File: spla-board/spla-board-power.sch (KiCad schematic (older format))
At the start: 17 parts, among them J10 J_3V3_EN, J11 J_5V_SWITCH, J12 J_POWER, J7 Barrel_Jack, J8 J_3V3_EN, J9 J_2V5_EN, U14 TLV73311PDBV, U7 MIC2025-1YM, U8 TLV73333PDBV, U9 TLV73325PDBV

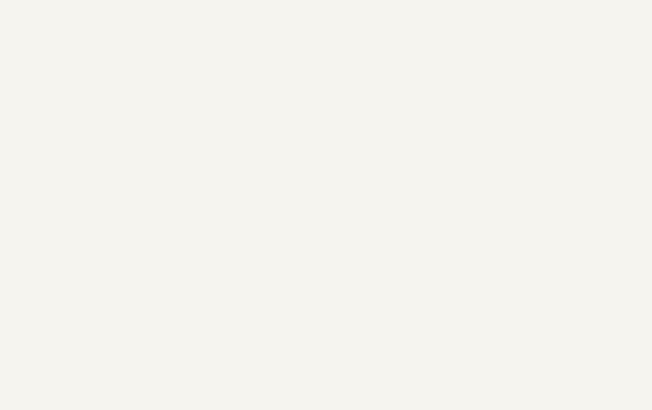
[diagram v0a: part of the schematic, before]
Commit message: pcb/schematic: Add plated mounting holes.
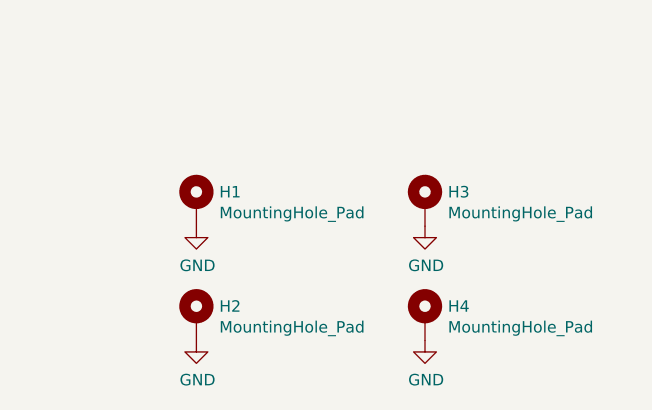
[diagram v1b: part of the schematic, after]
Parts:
- added H1, H2, H3, H4: MountingHole_Pad, MountingHole:MountingHole_3.2mm_M3_Pad, symbol Mechanical:MountingHole_Pad
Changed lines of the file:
@@
 Text Notes 3900 5600 0    50   ~ 0
 TODO: Swap these 300mA LDOs for AMS1117 parts.
+$Comp
+L Mechanical:MountingHole_Pad H?
+U 1 1 5E9F55D4
+P 13400 8150
+AR Path="/5E9F55D4" Ref="H?"  Part="1"
+AR Path="/5E50D39B/5E9F55D4" Ref="H1"  Part="1"
+F 0 "H1" H 13500 8199 50  0000 L CNN
+F 1 "MountingHole_Pad" H 13500 8108 50  0000 L CNN
+F 2 "MountingHole:MountingHole_3.2mm_M3_Pad" H 13400 8150 50  0001 C CNN
+F 3 "~" H 13400 8150 50  0001 C CNN
+	1    13400 8150
+	1    0    0    -1
+$EndComp
+$Comp
+L Mechanical:MountingHole_Pad H?
+U 1 1 5E9F55DA
+P 14400 8150
+AR Path="/5E9F55DA" Ref="H?"  Part="1"
+AR Path="/5E50D39B/5E9F55DA" Ref="H3"  Part="1"
+F 0 "H3" H 14500 8199 50  0000 L CNN
+F 1 "MountingHole_Pad" H 14500 8108 50  0000 L CNN
+F 2 "MountingHole:MountingHole_3.2mm_M3_Pad" H 14400 8150 50  0001 C CNN
+F 3 "~" H 14400 8150 50  0001 C CNN
+	1    14400 8150
+	1    0    0    -1
+$EndComp
+$Comp
+L Mechanical:MountingHole_Pad H?
+U 1 1 5E9F55E0
+P 13400 8650
+AR Path="/5E9F55E0" Ref="H?"  Part="1"
+AR Path="/5E50D39B/5E9F55E0" Ref="H2"  Part="1"
+F 0 "H2" H 13500 8699 50  0000 L CNN
+F 1 "MountingHole_Pad" H 13500 8608 50  0000 L CNN
+F 2 "MountingHole:MountingHole_3.2mm_M3_Pad" H 13400 8650 50  0001 C CNN
+F 3 "~" H 13400 8650 50  0001 C CNN
+	1    13400 8650
+	1    0    0    -1
+$EndComp
+$Comp
+L Mechanical:MountingHole_Pad H?
+U 1 1 5E9F55E6
+P 14400 8650
+AR Path="/5E9F55E6" Ref="H?"  Part="1"
+AR Path="/5E50D39B/5E9F55E6" Ref="H4"  Part="1"
+F 0 "H4" H 14500 8699 50  0000 L CNN
+F 1 "MountingHole_Pad" H 14500 8608 50  0000 L CNN
+F 2 "MountingHole:MountingHole_3.2mm_M3_Pad" H 14400 8650 50  0001 C CNN
+F 3 "~" H 14400 8650 50  0001 C CNN
+	1    14400 8650
+	1    0    0    -1
+$EndComp
+$Comp
+L power:GND #PWR?
+U 1 1 5E9F55EC
+P 13400 8250
+AR Path="/5E9F55EC" Ref="#PWR?"  Part="1"
+AR Path="/5E50D39B/5E9F55EC" Ref="#PWR0176"  Part="1"
+F 0 "#PWR0176" H 13400 8000 50  0001 C CNN
+F 1 "GND" H 13405 8077 50  0000 C CNN
+F 2 "" H 13400 8250 50  0001 C CNN
+F 3 "" H 13400 8250 50  0001 C CNN
+	1    13400 8250
+	1    0    0    -1
+$EndComp
+$Comp
+L power:GND #PWR?
+U 1 1 5E9F55F2
+P 14400 8250
+AR Path="/5E9F55F2" Ref="#PWR?"  Part="1"
+AR Path="/5E50D39B/5E9F55F2" Ref="#PWR0180"  Part="1"
+F 0 "#PWR0180" H 14400 8000 50  0001 C CNN
+F 1 "GND" H 14405 8077 50  0000 C CNN
+F 2 "" H 14400 8250 50  0001 C CNN
+F 3 "" H 14400 8250 50  0001 C CNN
+	1    14400 8250
+	1    0    0    -1
+$EndComp
+$Comp
+L power:GND #PWR?
+U 1 1 5E9F55F8
+P 13400 8750
+AR Path="/5E9F55F8" Ref="#PWR?"  Part="1"
+AR Path="/5E50D39B/5E9F55F8" Ref="#PWR0181"  Part="1"
+F 0 "#PWR0181" H 13400 8500 50  0001 C CNN
+F 1 "GND" H 13405 8577 50  0000 C CNN
+F 2 "" H 13400 8750 50  0001 C CNN
+F 3 "" H 13400 8750 50  0001 C CNN
+	1    13400 8750
+	1    0    0    -1
+$EndComp
+$Comp
+L power:GND #PWR?
+U 1 1 5E9F55FE
+P 14400 8750
+AR Path="/5E9F55FE" Ref="#PWR?"  Part="1"
+AR Path="/5E50D39B/5E9F55FE" Ref="#PWR0184"  Part="1"
+F 0 "#PWR0184" H 14400 8500 50  0001 C CNN
+F 1 "GND" H 14405 8577 50  0000 C CNN
+F 2 "" H 14400 8750 50  0001 C CNN
+F 3 "" H 14400 8750 50  0001 C CNN
+	1    14400 8750
+	1    0    0    -1
+$EndComp
 $EndSCHEMATC

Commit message: symbol/footprint/schematic: Redo power entirely to use ST1S10 and TLV733 parts.
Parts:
- removed J10, J8: J_3V3_EN, Connector_PinHeader_2.54mm:PinHeader_2x03_P2.54mm_Vertical, symbol Connector_Generic:Conn_02x03_Odd_Even
- removed J11: J_5V_SWITCH, Connector_PinHeader_2.54mm:PinHeader_2x03_P2.54mm_Vertical, symbol Connector_Generic:Conn_02x03_Odd_Even
- removed J9: J_2V5_EN, Connector_PinHeader_2.54mm:PinHeader_2x03_P2.54mm_Vertical, symbol Connector_Generic:Conn_02x03_Odd_Even
- removed TP6: TP_5V, TestPoint:TestPoint_Pad_D1.0mm, symbol Connector:TestPoint
- removed TP7: TP_3V3, TestPoint:TestPoint_Pad_D1.0mm, symbol Connector:TestPoint
- removed TP8: TP_2V5, TestPoint:TestPoint_Pad_D1.0mm, symbol Connector:TestPoint
- removed TP9: TP_1V1, TestPoint:TestPoint_Pad_D1.0mm, symbol Connector:TestPoint
- removed U7: MIC2025-1YM, Package_SO:SOIC-8_3.9x4.9mm_P1.27mm, symbol Power_Management:MIC2025-1YM
- removed U8: TLV73333PDBV, Package_TO_SOT_SMD:SOT-23-5, symbol Regulator_Linear:TLV73333PDBV
- added C28: 10uF, Capacitor_SMD:C_0805_2012Metric, symbol Device:C_Small
- added C29, C30, C31, C32, C35, C36, C41, C42: 0.1uF, Capacitor_SMD:C_0603_1608Metric, symbol Device:C_Small
- added C33, C34: 4.7uF, Capacitor_SMD:C_0603_1608Metric, symbol Device:C_Small
- added C37, C38, C39, C40: 22uF, Capacitor_SMD:C_0805_2012Metric, symbol Device:C_Small
- added L1, L2: 3.3uH, Inductor_SMD:L_Vishay_IHLP-2020, symbol Device:L
- added R26, R27, R28, R33, R34: 0, Resistor_SMD:R_0603_1608Metric, symbol Device:R_Small
- added R29: 5.23k, 1%, Resistor_SMD:R_0603_1608Metric, symbol Device:R_Small
- added R30, R32: 1k, 1%, Resistor_SMD:R_0603_1608Metric, symbol Device:R_Small
- added R31: 3.09k, 1%, Resistor_SMD:R_0603_1608Metric, symbol Device:R_Small
- added U7, U8: ST1S10PHR, SPLA:ST_PowerSO-8EP_4x5mm_P1.27mm_EP3.5x2.6mm, symbol SPLA:ST1S10PHR
- C13: value 0.1uF -> 10uF; footprint Capacitor_SMD:C_0603_1608Metric -> Capacitor_SMD:C_0805_2012Metric
- R12: value 10k -> 0
- TP5: value TP_5VD -> TP_12V
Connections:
- net labels added: +12V, PWR_12V, PWR_PRE_1V1, PWR_PRE_2V5, PWR_PRE_3V3, PWR_PRE_5V
- net labels removed: +5VD, PWR_5V_EN, PWR_OVERFLAG
- wire segments 99 -> 164
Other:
- note added: "SYNC = use internal 900kHz oscillator"
- note added: "V_OUT = ((0.8V / 1k) * 3.09k) + 0.8V = 3.272V"
- note added: "V_OUT = ((0.8V / 1k) * 5.23k) + 0.8V = 4.984V"
- note added: "~INH~ = Always On"
- note removed: "TODO: Swap these 300mA LDOs for AMS1117 parts."
- moved on the sheet: J12, J7, TP5

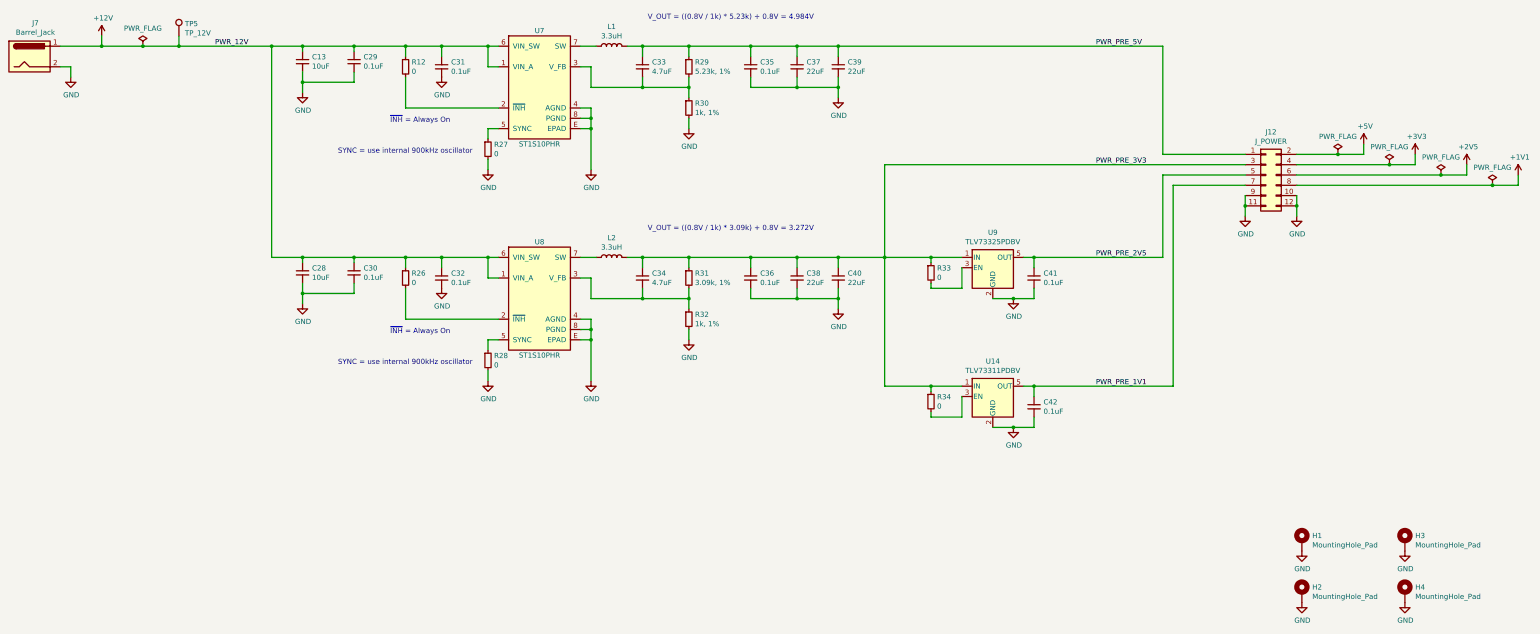
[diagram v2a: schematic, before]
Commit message: pcb/schematic: Partial work on power layout.
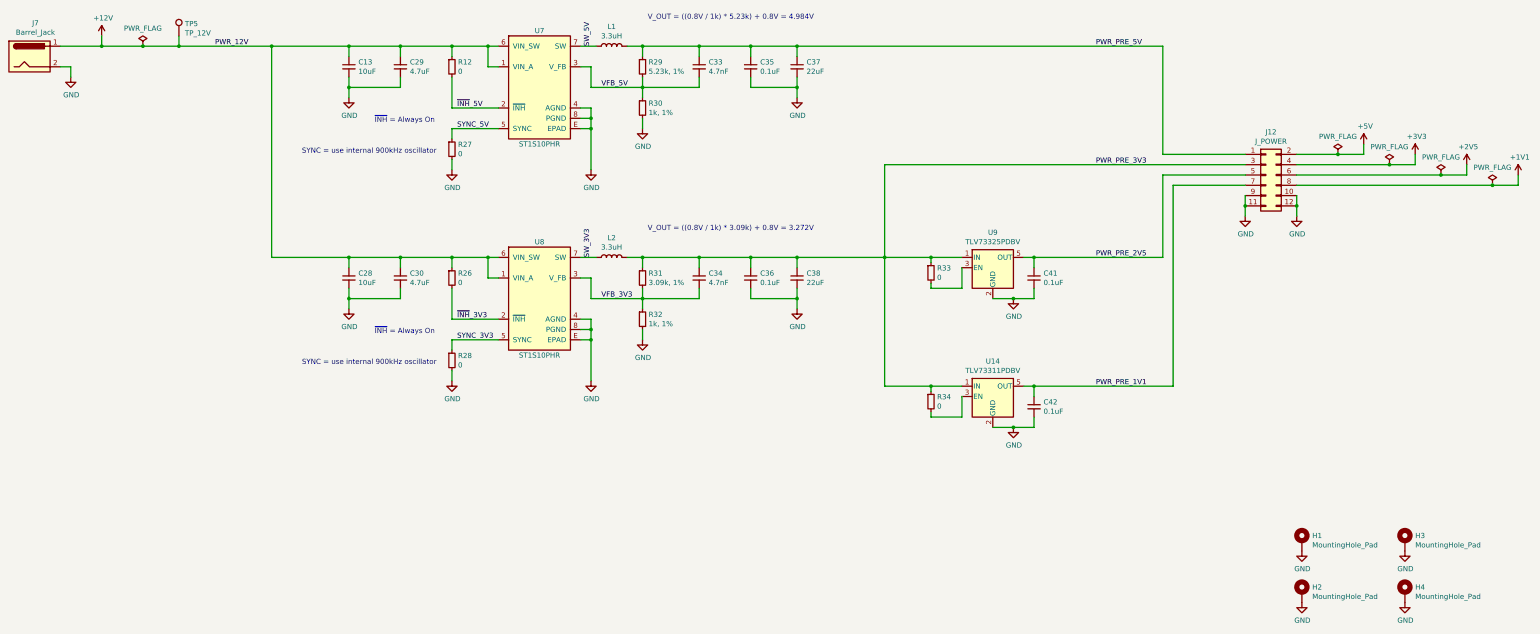
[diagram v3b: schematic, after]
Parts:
- removed C31, C32: 0.1uF, Capacitor_SMD:C_0603_1608Metric, symbol Device:C_Small
- removed C39, C40: 22uF, Capacitor_SMD:C_0805_2012Metric, symbol Device:C_Small
- C29, C30: value 0.1uF -> 4.7uF
- C33, C34: value 4.7uF -> 4.7nF
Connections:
- net ~INH~_5V: now reaches R12.2, U7.2 (~INH)
- net VFB_5V: now reaches C33.2, R29.2, R30.1, U7.3 (V_FB)
- net SYNC_5V: now reaches R27.1, U7.5 (SYNC)
- net SW_5V: now reaches L1.1, U7.7 (SW)
- net ~INH~_3V3: now reaches R26.2, U8.2 (~INH)
- net VFB_3V3: now reaches C34.2, R31.2, R32.1, U8.3 (V_FB)
- net SYNC_3V3: now reaches R28.1, U8.5 (SYNC)
- net SW_3V3: now reaches L2.1, U8.7 (SW)
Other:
- moved on the sheet: C13, C28, C29, C30, C33, C34, R12, R26, R27, R28, R29, R30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

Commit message: schematic/pcb: Rearrange 2.5V/1.1V jumpers; Move USB data liens to make space for power.
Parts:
- J12: footprint Connector_PinHeader_2.54mm:PinHeader_2x06_P2.54mm_Vertical -> Connector_PinHeader_2.54mm:PinHeader_2x07_P2.54mm_Vertical; symbol Connector_Generic:Conn_02x06_Odd_Even -> Connector_Generic:Conn_02x07_Odd_Even
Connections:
- net +1V1: now also C42.1, U14.5 (OUT); no longer J12.8 (Pin_8)
- net +2V5: now also C41.1, U9.5 (OUT); no longer J12.6 (Pin_6)
- net +3V3: now also J12.11 (Pin_11), J12.5 (Pin_5); no longer J12.4 (Pin_4)
- net +5V: now also J12.13 (Pin_13); no longer J12.2 (Pin_2)
- net GND: now also J12.1 (Pin_1), J12.2 (Pin_2), J12.3 (Pin_3), J12.4 (Pin_4); no longer J12.10 (Pin_10), J12.11 (Pin_11), J12.12 (Pin_12), J12.9 (Pin_9)
- net PWR_PRE_3V3: now also J12.10 (Pin_10), J12.12 (Pin_12), J12.6 (Pin_6), J12.8 (Pin_8); no longer J12.3 (Pin_3), R33.1, R34.1, U14.1 (IN), U9.1 (IN)
- net PWR_PRE_5V: now also J12.14 (Pin_14); no longer J12.1 (Pin_1)
- removed net PWR_PRE_1V1: C42.1, J12.7 (Pin_7), U14.5 (OUT)
- removed net PWR_PRE_2V5: C41.1, J12.5 (Pin_5), U9.5 (OUT)
- new net PWR_INTO_1V1: J12.7 (Pin_7), R34.1, U14.1 (IN)
- new net PWR_INTO_2V5: J12.9 (Pin_9), R33.1, U9.1 (IN)
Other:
- moved on the sheet: C41, C42, R33, R34, U14, U9

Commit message: pcb/schematic: Layout new power setup; tweak schematic to suit.
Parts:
- added TP6: TP_GND, TestPoint:TestPoint_Plated_Hole_D2.0mm, symbol Connector:TestPoint
- J12: footprint Connector_PinHeader_2.54mm:PinHeader_2x07_P2.54mm_Vertical -> Connector_PinHeader_2.54mm:PinHeader_2x08_P2.54mm_Vertical; symbol Connector_Generic:Conn_02x07_Odd_Even -> Connector_Generic:Conn_02x08_Odd_Even
- TP5: footprint TestPoint:TestPoint_Pad_D1.0mm -> TestPoint:TestPoint_Plated_Hole_D2.0mm
- renumbered C13 to C81, C37 to C82, C29 to C83, C33 to C84, C35 to C89, C28 to C91, C38 to C92, C30 to C93, C34 to C94, C36 to C99, R29 to R81, R30 to R82, R12 to R87, R27 to R88, R31 to R91, R32 to R92, R26 to R97, R28 to R98
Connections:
- net +3V3: now also J12.13 (Pin_13), J12.7 (Pin_7); no longer J12.11 (Pin_11), J12.5 (Pin_5)
- net +5V: now also J12.3 (Pin_3); no longer J12.13 (Pin_13)
- net GND: now also J12.15 (Pin_15), J12.16 (Pin_16), J12.5 (Pin_5), J12.6 (Pin_6), TP6.1; no longer J12.3 (Pin_3), J12.4 (Pin_4)
- net PWR_INTO_1V1: now also J12.11 (Pin_11); no longer J12.7 (Pin_7)
- net PWR_PRE_3V3: now also J12.14 (Pin_14); no longer J12.6 (Pin_6)
- net PWR_PRE_5V: now also J12.4 (Pin_4); no longer J12.14 (Pin_14)
- net PWR_EN_1V1: now reaches R34.2, U14.3 (EN)
- net PWR_EN_2V5: now reaches R33.2, U9.3 (EN)
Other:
- moved on the sheet: R33, R34

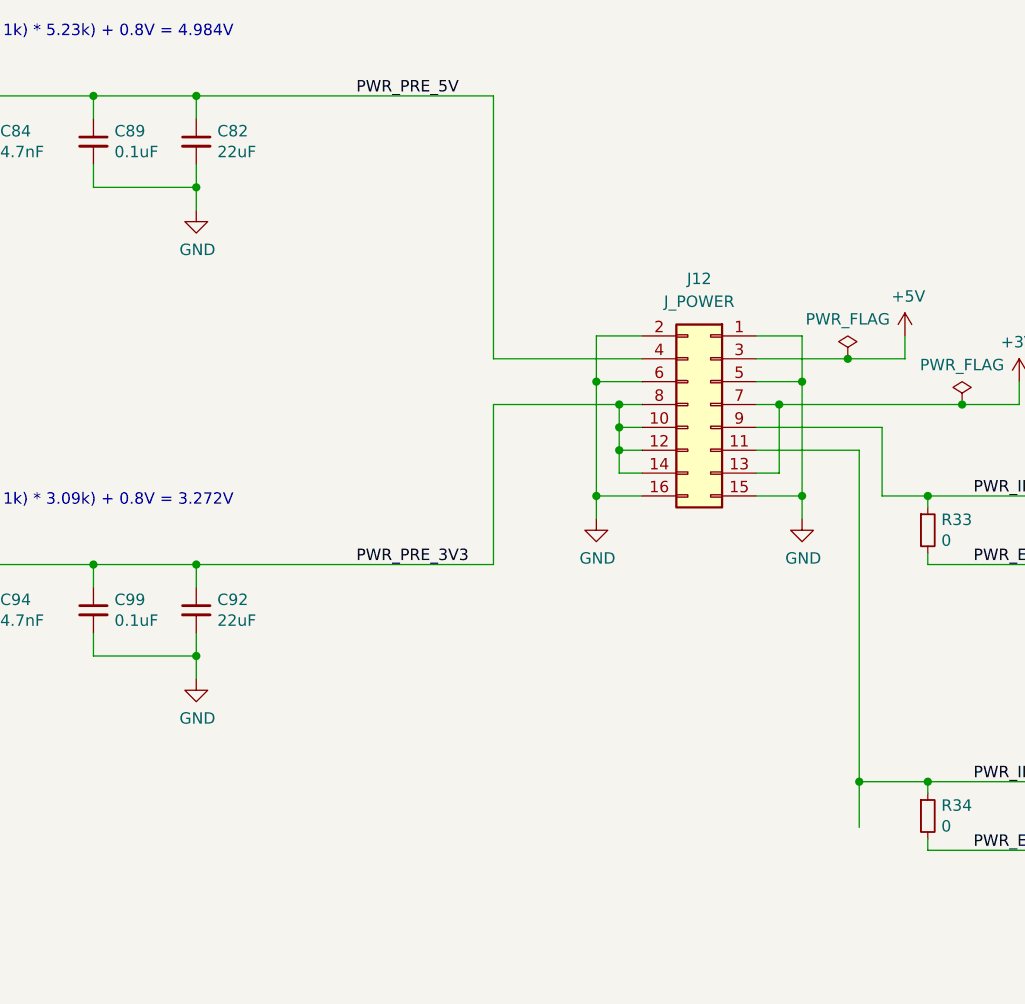
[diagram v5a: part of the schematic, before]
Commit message: schematic/pcb: Add LEDs to FTDI / FPGA / Power, for bringup and debugging.
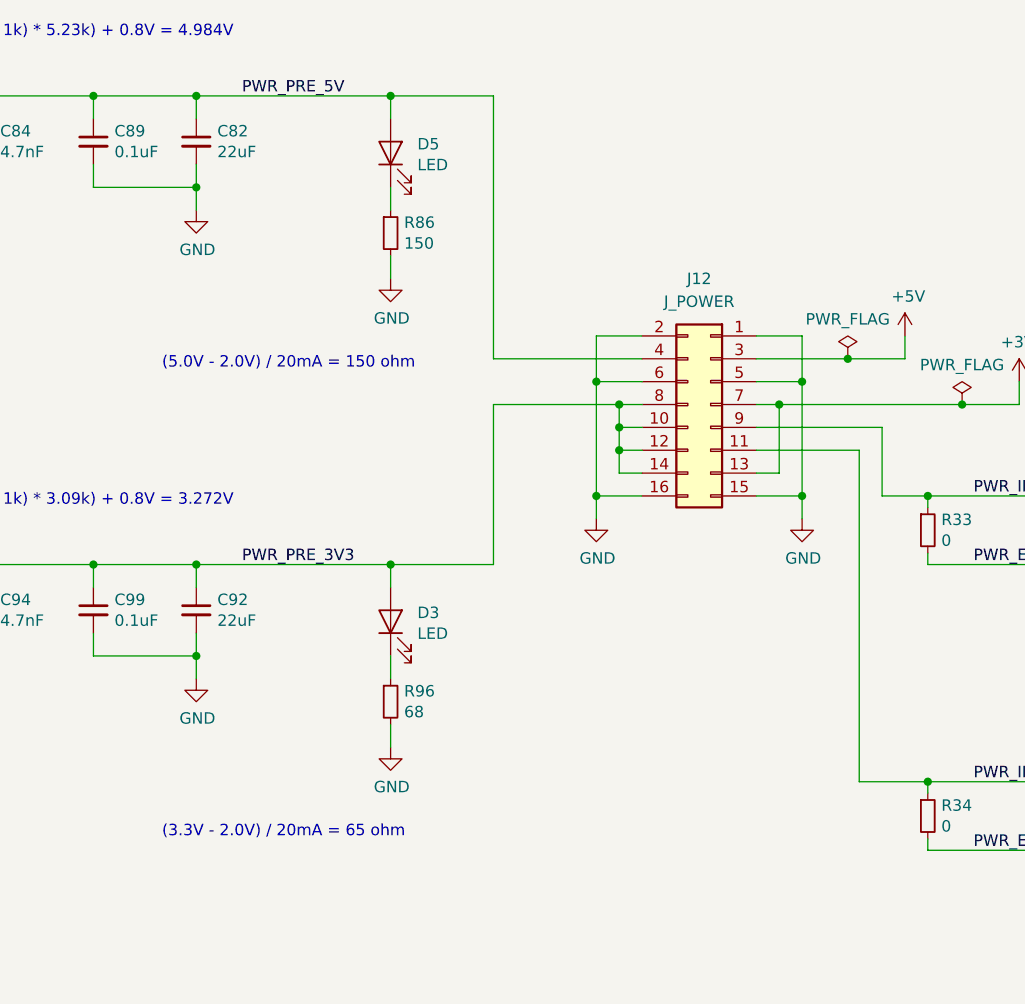
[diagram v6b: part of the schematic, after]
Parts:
- added D3, D5: LED, LED_SMD:LED_0805_2012Metric, symbol Device:LED
- added R86: 150, Resistor_SMD:R_0603_1608Metric, symbol Device:R_Small
- added R96: 68, Resistor_SMD:R_0603_1608Metric, symbol Device:R_Small
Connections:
- net GND: now also R86.2, R96.2
- net PWR_PRE_3V3: now also D3.2 (A)
- net PWR_PRE_5V: now also D5.2 (A)
- new net: D5.1 (K), R86.1
- new net: D3.1 (K), R96.1
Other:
- note added: "(3.3V - 2.0V) / 20mA = 65 ohm"
- note added: "(5.0V - 2.0V) / 20mA = 150 ohm"
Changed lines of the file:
@@
 Text Label 2850 3350 0    50   ~ 0
 PWR_12V
-Text Label 9200 3350 0    50   ~ 0
+Text Label 8700 3350 0    50   ~ 0
 PWR_PRE_5V
-Text Label 9200 5400 0    50   ~ 0
+Text Label 8700 5400 0    50   ~ 0
 PWR_PRE_3V3
 Wire Wire Line
@@
 	7000 3850 7000 3750
 Wire Wire Line
-	8500 3350 9800 3350
+	8500 3350 9350 3350
 Wire Wire Line
 	6500 5800 7000 5800
@@
 	8050 5800 8500 5800
 Wire Wire Line
-	8500 5400 9800 5400
+	8500 5400 9350 5400
 Wire Wire Line
 	10350 4900 10350 4800
@@
 Wire Wire Line
 	12100 4700 11850 4700
-Connection ~ 11400 6350
-Wire Wire Line
-	11400 6350 11400 6550
 Wire Wire Line
 	12100 4600 12100 4700
@@
 	2500 3650 1450 3650
 Connection ~ 2500 3650
+$Comp
+L Device:LED D?
+U 1 1 5EB36971
+P 9350 3600
+AR Path="/5E4F712F/5EB36971" Ref="D?"  Part="1"
+AR Path="/5E50D39B/5EB36971" Ref="D5"  Part="1"
+F 0 "D5" V 9389 3483 50  0000 R CNN
+F 1 "LED" V 9298 3483 50  0000 R CNN
+F 2 "LED_SMD:LED_0805_2012Metric" H 9350 3600 50  0001 C CNN
+F 3 "~" H 9350 3600 50  0001 C CNN
+	1    9350 3600
+	0    -1   -1   0
+$EndComp
+$Comp
+L Device:R_Small R?
+U 1 1 5EB36977
+P 9350 3950
+AR Path="/5E4F712F/5EB36977" Ref="R?"  Part="1"
+AR Path="/5E50D39B/5EB36977" Ref="R86"  Part="1"
+F 0 "R86" H 9409 3996 50  0000 L CNN
+F 1 "150" H 9409 3905 50  0000 L CNN
+F 2 "Resistor_SMD:R_0603_1608Metric" H 9350 3950 50  0001 C CNN
+F 3 "~" H 9350 3950 50  0001 C CNN
+	1    9350 3950
+	1    0    0    -1
+$EndComp
+Wire Wire Line
+	9350 3750 9350 3850
+Wire Wire Line
+	9350 4050 9350 4150
+$Comp
+L power:GND #PWR?
+U 1 1 5EB3697F
+P 9350 4150
+AR Path="/5E4F712F/5EB3697F" Ref="#PWR?"  Part="1"
+AR Path="/5E50D39B/5EB3697F" Ref="#PWR0190"  Part="1"
+F 0 "#PWR0190" H 9350 3900 50  0001 C CNN
+F 1 "GND" H 9355 3977 50  0000 C CNN
+F 2 "" H 9350 4150 50  0001 C CNN
+F 3 "" H 9350 4150 50  0001 C CNN
+	1    9350 4150
+	1    0    0    -1
+$EndComp
+Text Notes 8350 4550 0    50   ~ 0
+(5.0V - 2.0V) / 20mA = 150 ohm
+Wire Wire Line
+	9350 3350 9350 3450
+$Comp
+L Device:LED D?
+U 1 1 5EB3D482
+P 9350 5650
+AR Path="/5E4F712F/5EB3D482" Ref="D?"  Part="1"
+AR Path="/5E50D39B/5EB3D482" Ref="D3"  Part="1"
+F 0 "D3" V 9389 5533 50  0000 R CNN
+F 1 "LED" V 9298 5533 50  0000 R CNN
+F 2 "LED_SMD:LED_0805_2012Metric" H 9350 5650 50  0001 C CNN
+F 3 "~" H 9350 5650 50  0001 C CNN
+	1    9350 5650
+	0    -1   -1   0
+$EndComp
+$Comp
+L Device:R_Small R?
+U 1 1 5EB3D48C
+P 9350 6000
+AR Path="/5E4F712F/5EB3D48C" Ref="R?"  Part="1"
+AR Path="/5E50D39B/5EB3D48C" Ref="R96"  Part="1"
+F 0 "R96" H 9409 6046 50  0000 L CNN
+F 1 "68" H 9409 5955 50  0000 L CNN
+F 2 "Resistor_SMD:R_0603_1608Metric" H 9350 6000 50  0001 C CNN
+F 3 "~" H 9350 6000 50  0001 C CNN
+	1    9350 6000
+	1    0    0    -1
+$EndComp
+Wire Wire Line
+	9350 5800 9350 5900
+Wire Wire Line
+	9350 6100 9350 6200
+$Comp
+L power:GND #PWR?
+U 1 1 5EB3D498
+P 9350 6200
+AR Path="/5E4F712F/5EB3D498" Ref="#PWR?"  Part="1"
+AR Path="/5E50D39B/5EB3D498" Ref="#PWR0191"  Part="1"
+F 0 "#PWR0191" H 9350 5950 50  0001 C CNN
+F 1 "GND" H 9355 6027 50  0000 C CNN
+F 2 "" H 9350 6200 50  0001 C CNN
+F 3 "" H 9350 6200 50  0001 C CNN
+	1    9350 6200
+	1    0    0    -1
+$EndComp
+Text Notes 8350 6600 0    50   ~ 0
+(3.3V - 2.0V) / 20mA = 65 ohm
+Wire Wire Line
+	9350 5400 9350 5500
+Connection ~ 9350 5400
+Wire Wire Line
+	9350 5400 9800 5400
+Connection ~ 9350 3350
+Wire Wire Line
+	9350 3350 9800 3350
 $EndSCHEMATC
